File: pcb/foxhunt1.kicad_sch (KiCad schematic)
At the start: 8 parts, among them Q8 AO3400A, Q9 AO3400A, U10 LM74610, U7 LM74610

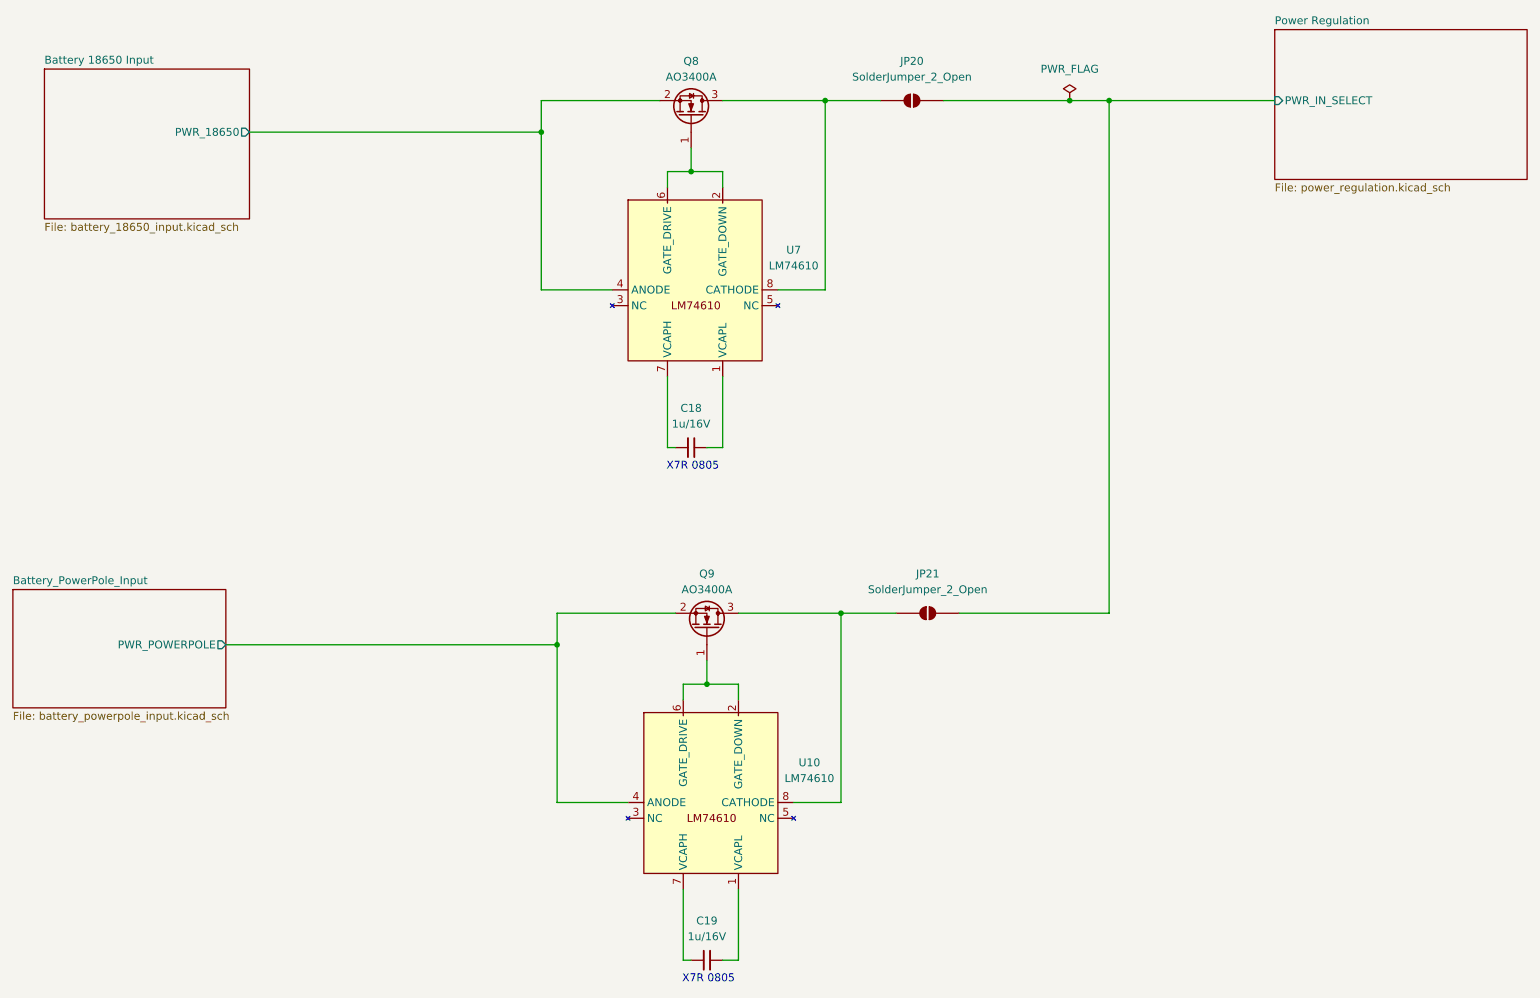
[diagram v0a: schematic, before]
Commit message: Add ESP32-S3 MCU sheet and CH340C USB-UART programming bridge
Restructures the schematic hierarchy: root sheet now hosts three
top-level sheets (Power, mcu-esp32, USB-C Programming UART) instead of
the old flat layout, with the battery/12V ORing-FET merge circuit
moved into its own dedicated Power sheet. Adds the ESP32-S3-WROOM-1
MCU sheet (native USB-C connector stubbed in but not yet wired) and a
CH340C-based USB-UART bridge with auto-reset/bootloader transistor
circuit for programming.

This is a work-in-progress checkpoint — several nets in the new sheets
(MCU decoupling, CH340C power, auto-reset routing, ORing FET gate
drive) still need wiring before ERC will be clean; see prior review
notes for the punch list.

Co-Authored-By: Claude Sonnet 5 <noreply@anthropic.com>
Claude-Session: https://claude.ai/code/session_01LwTJQ9pyVNMigbu4uLMh8c
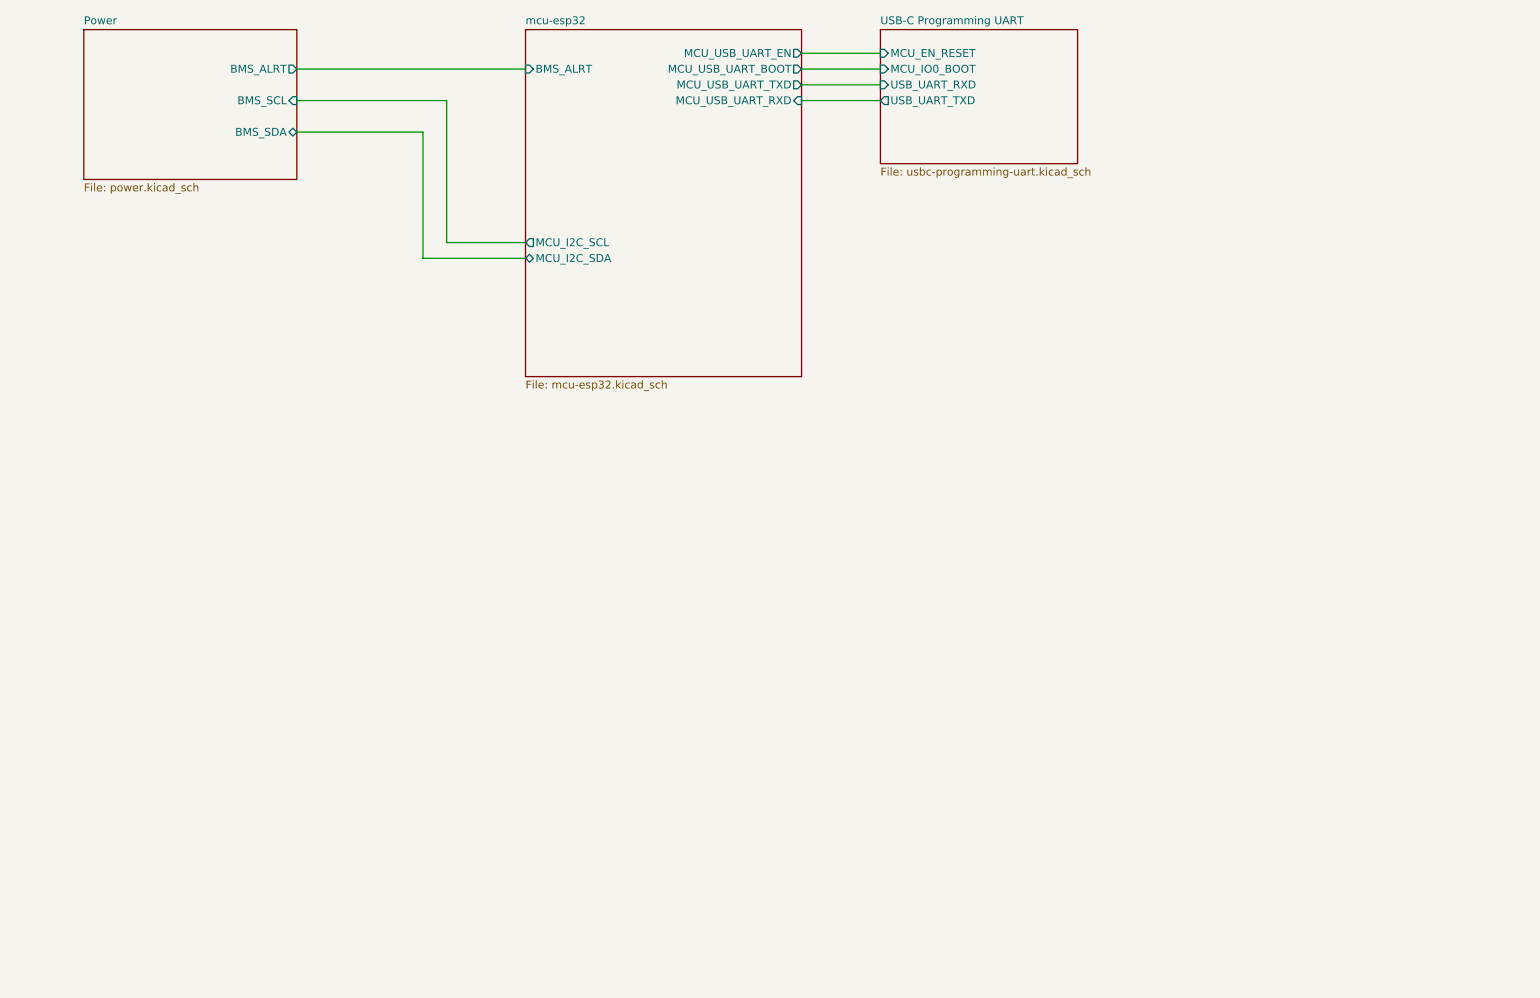
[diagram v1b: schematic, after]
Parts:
- removed C18, C19: 1u/16V, Capacitor_SMD:C_0805_2012Metric, symbol Device:C_Small
- removed JP20, JP21: SolderJumper_2_Open, Jumper:SolderJumper-2_P1.3mm_Open_TrianglePad1.0x1.5mm, symbol Jumper:SolderJumper_2_Open
- removed Q8, Q9: AO3400A, Package_TO_SOT_SMD:SOT-23, symbol Transistor_FET:AO3400A
- removed U10, U7: LM74610, Package_SO:VSSOP-8_3x3mm_P0.65mm, symbol kicad_gx_library:LM74610
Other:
- removed sheet Battery 18650 Input
- removed sheet Battery_PowerPole_Input
- removed sheet Power Regulation
- added sheet Power (power.kicad_sch)
- added sheet USB-C Programming UART (usbc-programming-uart.kicad_sch)
- added sheet mcu-esp32 (mcu-esp32.kicad_sch)
- note removed: "X7R 0805"
